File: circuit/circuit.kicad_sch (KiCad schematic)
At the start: 8 parts, among them M1 Motor_DC, SW2 SWITCH

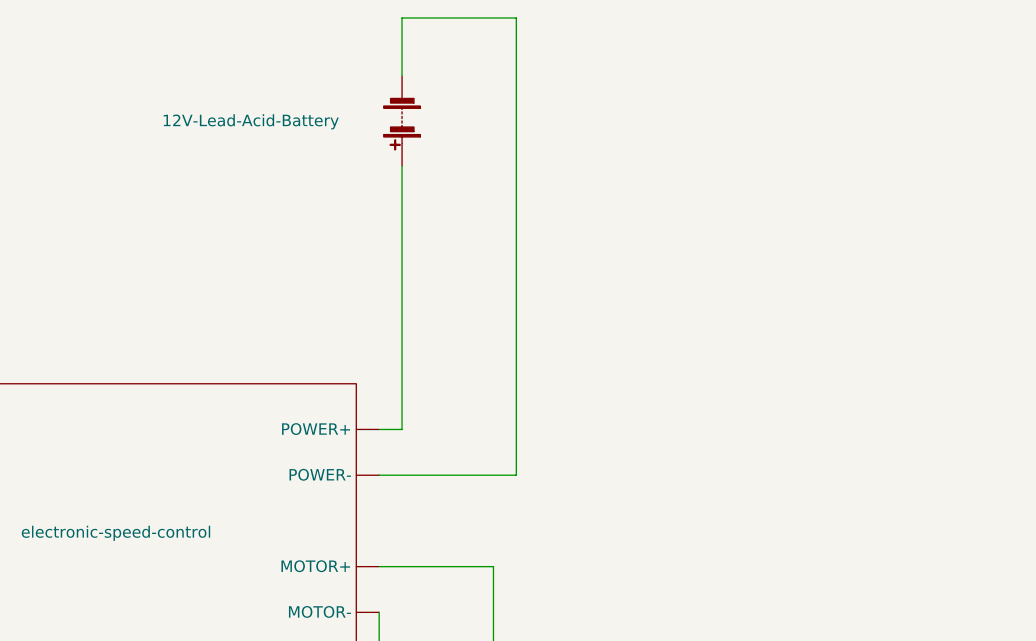
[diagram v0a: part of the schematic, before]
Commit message: add solar cells and remove one motor
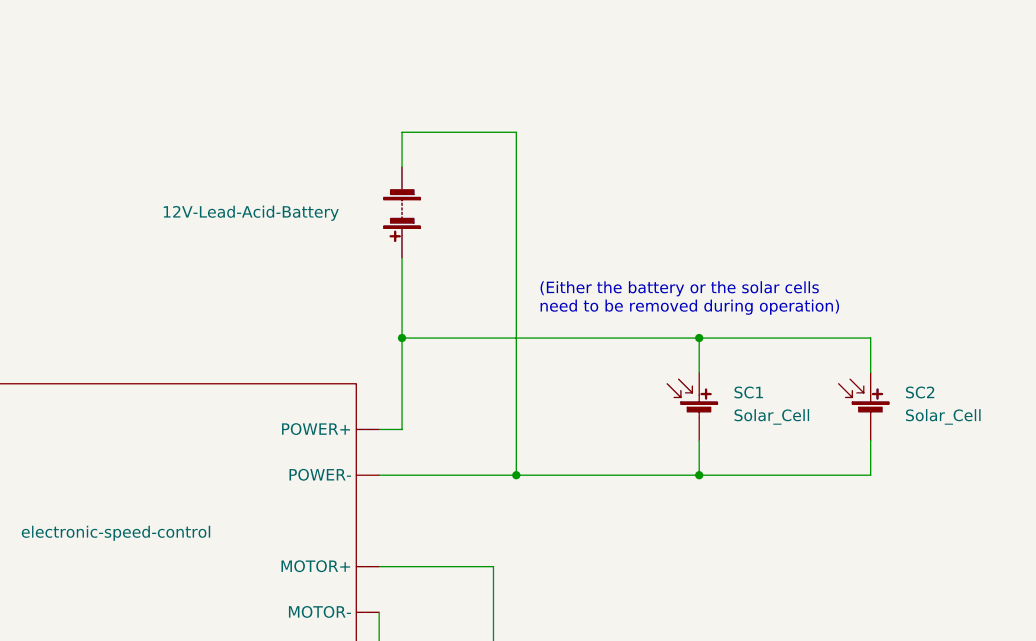
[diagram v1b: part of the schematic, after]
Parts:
- added SC1, SC2: Solar_Cell, symbol Device:Solar_Cell
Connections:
- net at 12V-Lead-Acid-Battery.1 (+), electronic-speed-control. (PWM): now also SC1.1 (+), SC2.1 (+)
- net at 12V-Lead-Acid-Battery.2 (-), electronic-speed-control. (PWM): now also SC1.2 (-), SC2.2 (-)
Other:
- note added: "(Either the battery or the solar cells need to be removed during operation)"
- moved on the sheet: 12V-Lead-Acid-Battery
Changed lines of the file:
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@@
   (title_block
     (title "Solar Boat Electronics")
-    (date "2023-03-31")
-    (rev "2")
+    (date "2023-04-01")
+    (rev "3")
     (company "Created by Ethan Cheng")
     (comment 1 "or send a letter to Creative Commons, PO Box 1866, Mountain View, CA 94042, USA.")
@@
     (comment 4 "This work is licensed under the Creative Commons Attribution-ShareAlike 4.0 International")
   )
+  (junction (at 201.93 74.93) (diameter 0) (color 0 0 0 0)
+  )
   (junction (at 92.71 130.81) (diameter 0) (color 0 0 0 0)
   )
   (junction (at 143.51 142.24) (diameter 0) (color 0 0 0 0)
   )
+  (junction (at 189.23 59.69) (diameter 0) (color 0 0 0 0)
+  )
+  (junction (at 222.25 59.69) (diameter 0) (color 0 0 0 0)
+  )
   (junction (at 114.3 142.24) (diameter 0) (color 0 0 0 0)
+  )
+  (junction (at 222.25 74.93) (diameter 0) (color 0 0 0 0)
   )
   (no_connect (at 119.38 120.65))
@@
     (stroke (width 0) (type default))
   )
-  (wire (pts (xy 189.23 40.64) (xy 189.23 69.85))
+  (wire (pts (xy 189.23 50.8) (xy 189.23 59.69))
     (stroke (width 0) (type default))
   )
@@
     (stroke (width 0) (type default))
   )
+  (wire (pts (xy 222.25 59.69) (xy 241.3 59.69))
+    (stroke (width 0) (type default))
+  )
   (wire (pts (xy 186.69 85.09) (xy 199.39 85.09))
     (stroke (width 0) (type default))
@@
     (stroke (width 0) (type default))
   )
-  (wire (pts (xy 189.23 24.13) (xy 189.23 30.48))
+  (wire (pts (xy 189.23 36.83) (xy 189.23 40.64))
     (stroke (width 0) (type default))
   )
@@
     (stroke (width 0) (type default))
   )
-  (wire (pts (xy 201.93 24.13) (xy 189.23 24.13))
+  (wire (pts (xy 201.93 36.83) (xy 189.23 36.83))
     (stroke (width 0) (type default))
   )
@@
     (stroke (width 0) (type default))
   )
+  (wire (pts (xy 201.93 74.93) (xy 222.25 74.93))
+    (stroke (width 0) (type default))
+  )
   (wire (pts (xy 199.39 85.09) (xy 199.39 110.49))
     (stroke (width 0) (type default))
@@
     (stroke (width 0) (type default))
   )
+  (wire (pts (xy 241.3 71.12) (xy 241.3 74.93))
+    (stroke (width 0) (type default))
+  )
+  (wire (pts (xy 241.3 59.69) (xy 241.3 63.5))
+    (stroke (width 0) (type default))
+  )
   (wire (pts (xy 99.06 85.09) (xy 105.41 85.09))
     (stroke (width 0) (type default))
@@
     (stroke (width 0) (type default))
   )
+  (wire (pts (xy 189.23 59.69) (xy 222.25 59.69))
+    (stroke (width 0) (type default))
+  )
   (wire (pts (xy 127 114.3) (xy 127 120.65))
     (stroke (width 0) (type default))
@@
     (stroke (width 0) (type default))
   )
+  (wire (pts (xy 222.25 71.12) (xy 222.25 74.93))
+    (stroke (width 0) (type default))
+  )
   (wire (pts (xy 139.7 130.81) (xy 143.51 130.81))
     (stroke (width 0) (type default))
@@
     (stroke (width 0) (type default))
   )
-  (wire (pts (xy 201.93 74.93) (xy 201.93 24.13))
+  (wire (pts (xy 201.93 74.93) (xy 201.93 36.83))
     (stroke (width 0) (type default))
   )
@@
     (stroke (width 0) (type default))
   )
+  (wire (pts (xy 222.25 63.5) (xy 222.25 59.69))
+    (stroke (width 0) (type default))
+  )
+  (wire (pts (xy 189.23 59.69) (xy 189.23 69.85))
+    (stroke (width 0) (type default))
+  )
   (wire (pts (xy 99.06 130.81) (xy 92.71 130.81))
     (stroke (width 0) (type default))
   )
+  (wire (pts (xy 222.25 74.93) (xy 241.3 74.93))
+    (stroke (width 0) (type default))
+  )
   (wire (pts (xy 132.08 114.3) (xy 132.08 120.65))
     (stroke (width 0) (type default))
@@
     (stroke (width 0) (type default))
   )
+  (text "(Either the battery or the solar cells\nneed to be removed during operation)"
+    (at 204.47 57.15 0)
+    (effects (font (size 1.27 1.27)) (justify left bottom))
+  )
   (label "DB6" (at 105.41 82.55 180) (fields_autoplaced)
     (effects (font (size 1.27 1.27)) (justify right bottom))
@@
     (effects (font (size 1.27 1.27)) (justify right bottom))
   )
-  (symbol (lib_id "Device:Battery") (at 189.23 35.56 180) (unit 1)
+  (symbol (lib_id "Device:Battery") (at 189.23 45.72 180) (unit 1)
     (in_bom yes) (on_board yes) (dnp no)
-    (property "Reference" "12V-Lead-Acid-Battery" (at 162.56 35.56 0)
+    (property "Reference" "12V-Lead-Acid-Battery" (at 162.56 45.72 0)
       (effects (font (size 1.27 1.27)) (justify right))
     )
-    (property "Value" "Battery" (at 193.04 37.846 0)
+    (property "Value" "Battery" (at 193.04 48.006 0)
       (effects (font (size 1.27 1.27)) (justify right) hide)
     )
-    (property "Footprint" "" (at 189.23 37.084 90)
-      (effects (font (size 1.27 1.27)) hide)
-    )
-    (property "Datasheet" "~" (at 189.23 37.084 90)
+    (property "Footprint" "" (at 189.23 47.244 90)
+      (effects (font (size 1.27 1.27)) hide)
+    )
+    (property "Datasheet" "~" (at 189.23 47.244 90)
       (effects (font (size 1.27 1.27)) hide)
     )
@@
     )
   )
+  (symbol (lib_id "Device:Solar_Cell") (at 222.25 68.58 0) (unit 1)
+    (in_bom yes) (on_board yes) (dnp no) (fields_autoplaced)
+    (property "Reference" "SC1" (at 226.06 65.786 0)
+      (effects (font (size 1.27 1.27)) (justify left))
+    )
+    (property "Value" "Solar_Cell" (at 226.06 68.326 0)
+      (effects (font (size 1.27 1.27)) (justify left))
+    )
+    (property "Footprint" "" (at 222.25 67.056 90)
+      (effects (font (size 1.27 1.27)) hide)
+    )
+    (property "Datasheet" "~" (at 222.25 67.056 90)
+      (effects (font (size 1.27 1.27)) hide)
+    )
+    (pin "1")
+    (pin "2")
+    (instances
+      (project "circuit"
+        (path "/a7f62f14-9e74-4202-9309-056814b6f529"
+          (reference "SC1") (unit 1)
+        )
+      )
+    )
+  )
   (symbol (lib_id "power:GND") (at 129.54 69.85 270) (unit 1)
     (in_bom yes) (on_board yes) (dnp no) (fields_autoplaced)
@@
         )
       )
+    )
+  )
+  (symbol (lib_id "Device:Solar_Cell") (at 241.3 68.58 0) (unit 1)
+    (in_bom yes) (on_board yes) (dnp no) (fields_autoplaced)
+    (property "Reference" "SC2" (at 245.11 65.786 0)
+      (effects (font (size 1.27 1.27)) (justify left))
+    )
+    (property "Value" "Solar_Cell" (at 245.11 68.326 0)
+      (effects (font (size 1.27 1.27)) (justify left))
+    )
+    (property "Footprint" "" (at 241.3 67.056 90)
+      (effects (font (size 1.27 1.27)) hide)
+    )
+    (property "Datasheet" "~" (at 241.3 67.056 90)
+      (effects (font (size 1.27 1.27)) hide)
+    )
+    (pin "1")
+    (pin "2")
+    (instances
+      (project "circuit"
+        (path "/a7f62f14-9e74-4202-9309-056814b6f529"
+          (reference "SC2") (unit 1)
+        )
+      )

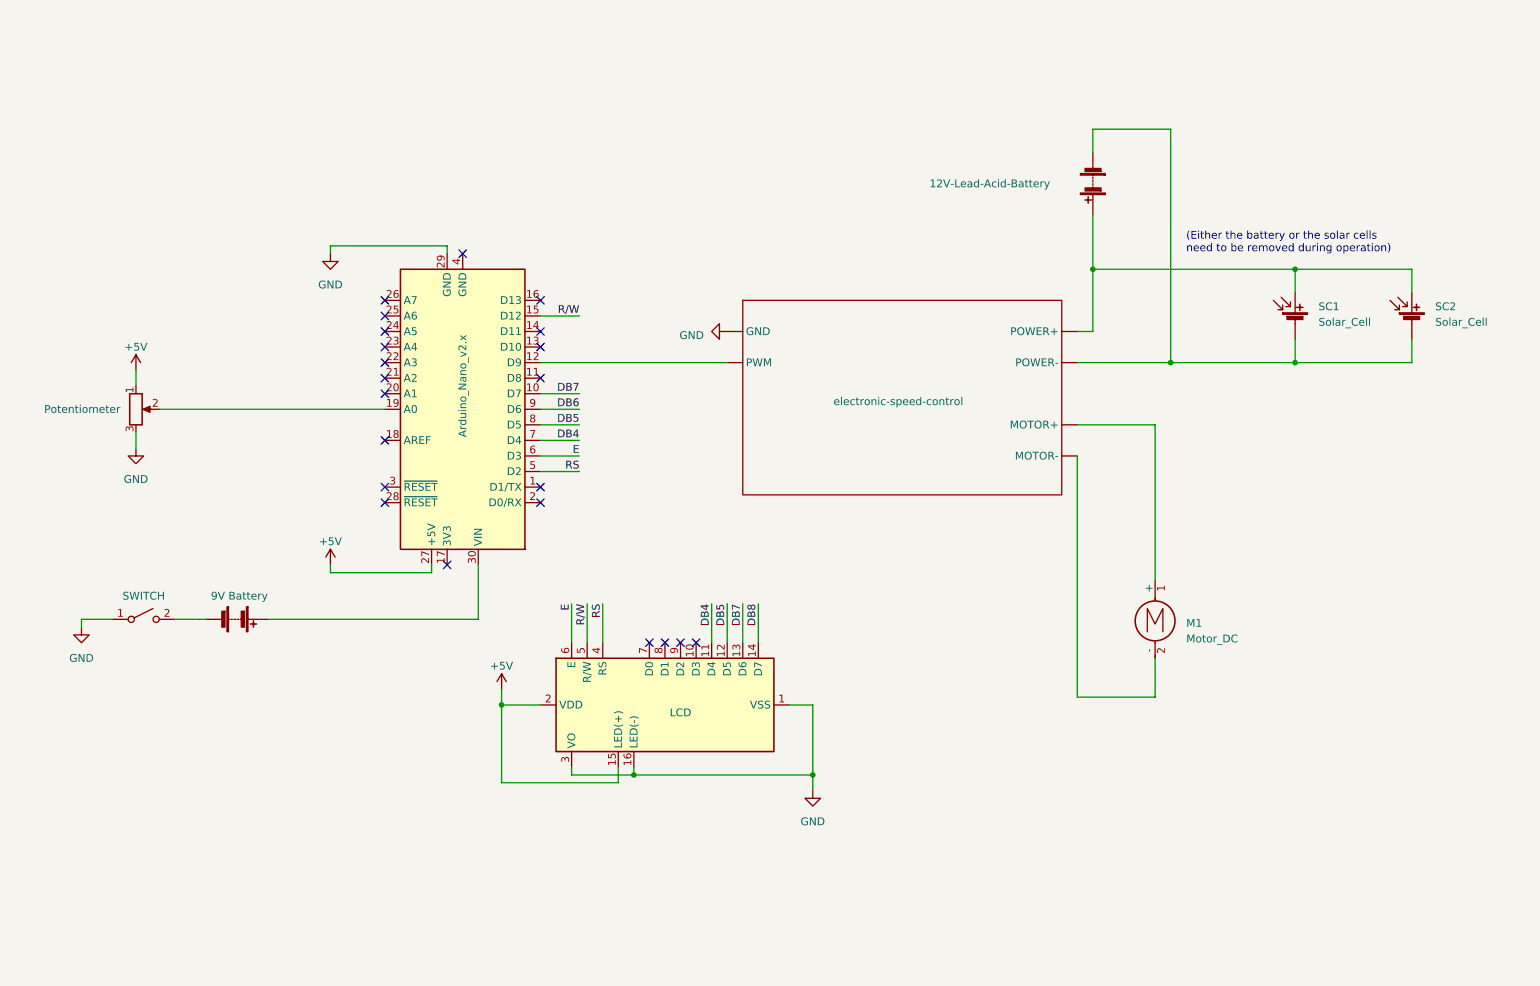
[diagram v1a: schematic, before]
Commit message: reorganize parts and fix typo in net label
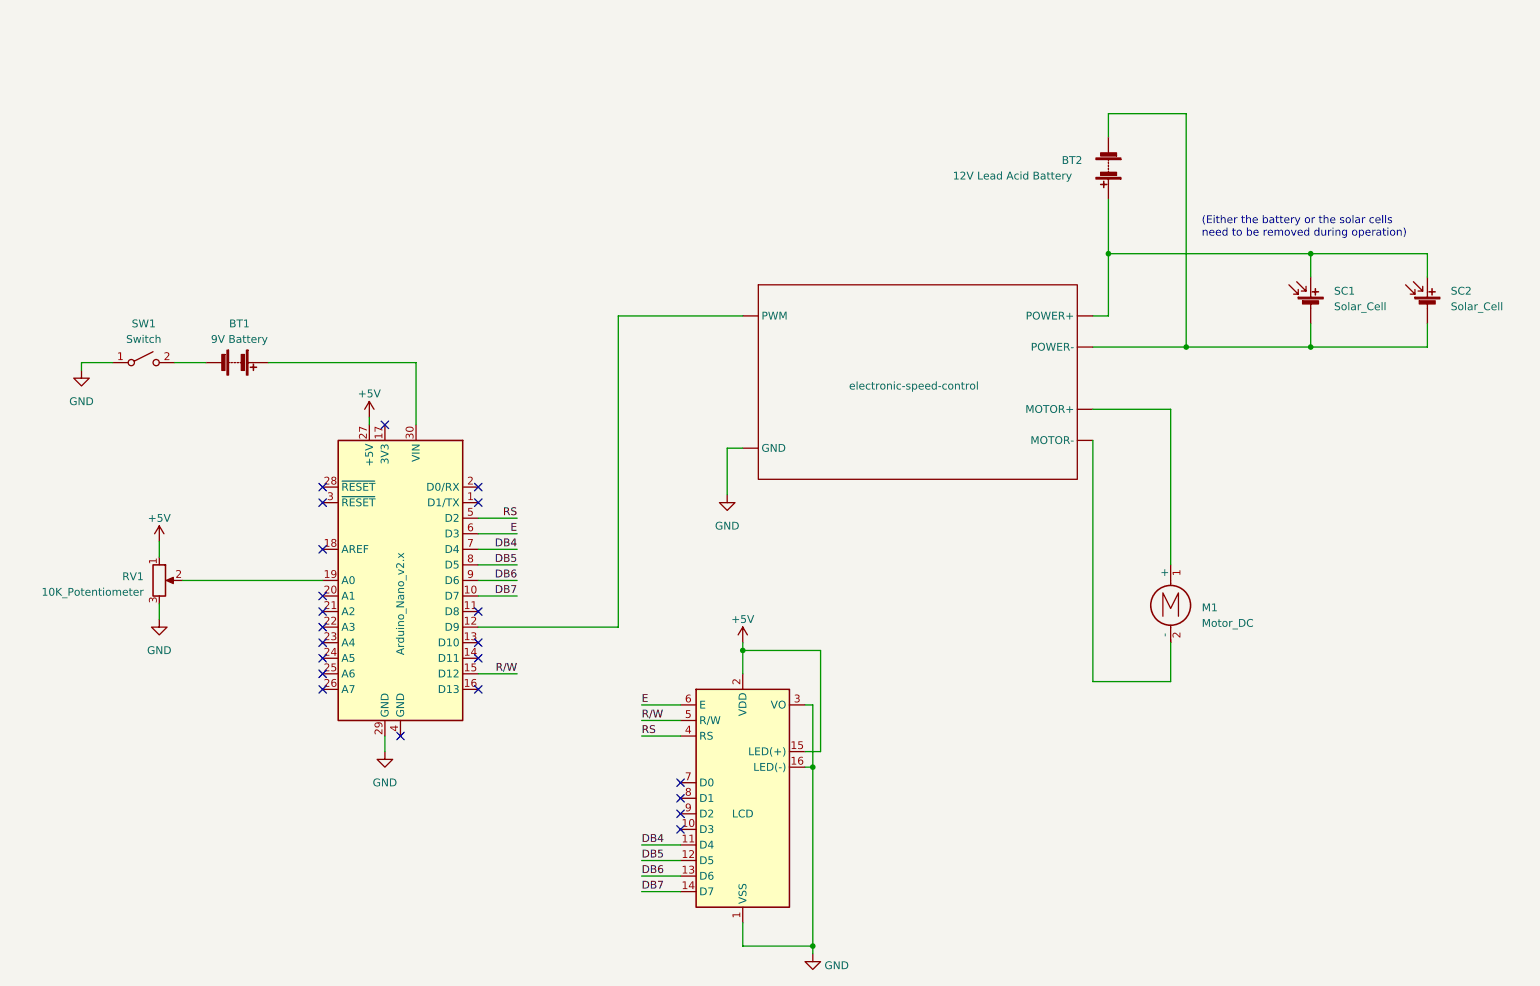
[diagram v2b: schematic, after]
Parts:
- removed 12V-Lead-Acid-Battery: Battery, symbol Device:Battery
- removed RV2: Potentiometer, symbol Device:R_Potentiometer
- removed SW2: SWITCH, symbol Switch:SW_SPST
- added BT1: 9V Battery, symbol Device:Battery
- added RV1: 10K_Potentiometer, symbol Device:R_Potentiometer
- added SW1: Switch, symbol Switch:SW_SPST
- BT2: value 9V Battery -> 12V Lead Acid Battery
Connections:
- net DB8 is gone; now on net DB7: DS2.14 (D7)
- net +5V: now also RV1.1
- net DB6: now also DS2.13 (D6)
- net DB7: no longer DS2.13 (D6)
- net GND: now also RV1.3, SW1.1 (A)
- net at SC1.1 (+), SC2.1 (+), electronic-speed-control. (PWM): now also BT2.1 (+)
- net at SC1.2 (-), SC2.2 (-), electronic-speed-control. (PWM): now also BT2.2 (-)
- net at A2.19 (A0): now also RV1.2
- net at A2.30 (VIN): now also BT1.1 (+); no longer BT2.1 (+)
- new net: BT1.2 (-), SW1.2 (B)
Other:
- moved on the sheet: M1, SC1, SC2, electronic-speed-control

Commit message: add emergency switches and step-down converter
One kill switch and one dead man's switch.
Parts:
- added DCDC1: ~, symbol ESC:step-down_converter
- added SW2: Kill Switch, symbol Switch:SW_SPST
- added SW3: Dead Man's Switch, symbol Switch:SW_SPST
- BT1: value 9V Battery -> 9V
- BT2: value 12V Lead Acid Battery -> 12V Lead Acid
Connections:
- net at SC1.1 (+), SC2.1 (+): now also DCDC1. (VOUT); no longer BT2.1 (+), electronic-speed-control. (PWM)
- net at SC1.2 (-), SC2.2 (-): now also DCDC1. (VOUT); no longer BT2.2 (-), electronic-speed-control. (PWM)
- new net: BT2.1 (+), DCDC1. (VOUT), electronic-speed-control. (PWM)
- new net: BT2.2 (-), DCDC1. (VOUT), SW3.2 (B)
- new net: SW2.1 (A), electronic-speed-control. (PWM)
- new net: SW2.2 (B), SW3.1 (A)
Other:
- note added: "(Either the battery or the solar cells can be removed during operation)"
- note removed: "(Either the battery or the solar cells need to be removed during operation)"
- moved on the sheet: M1, SC1, SC2
